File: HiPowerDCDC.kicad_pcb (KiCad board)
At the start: 2 copper layers, 125.8 x 100 mm, 70 parts, among them J1 Conn_01x01, J2 Conn_01x01, J3 Conn_01x01, J4 Conn_01x01, J5 Conn_01x04, J6 Conn_01x02, J7 12V vent., Q1 WMJ38N60, Q2 WMJ38N60, SW1 SW_Push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

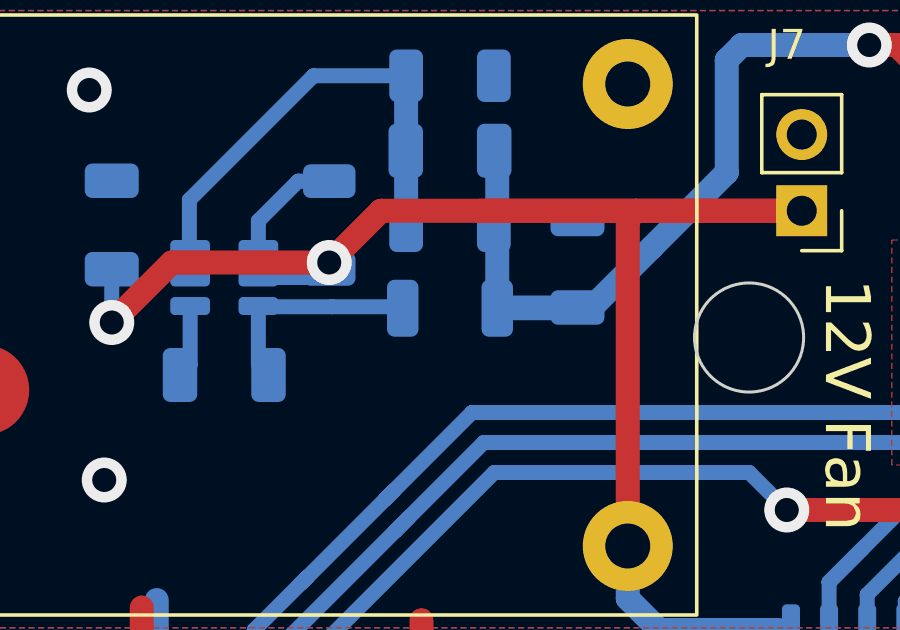
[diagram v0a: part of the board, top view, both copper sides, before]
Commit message: Increased DCDC inductor footprint
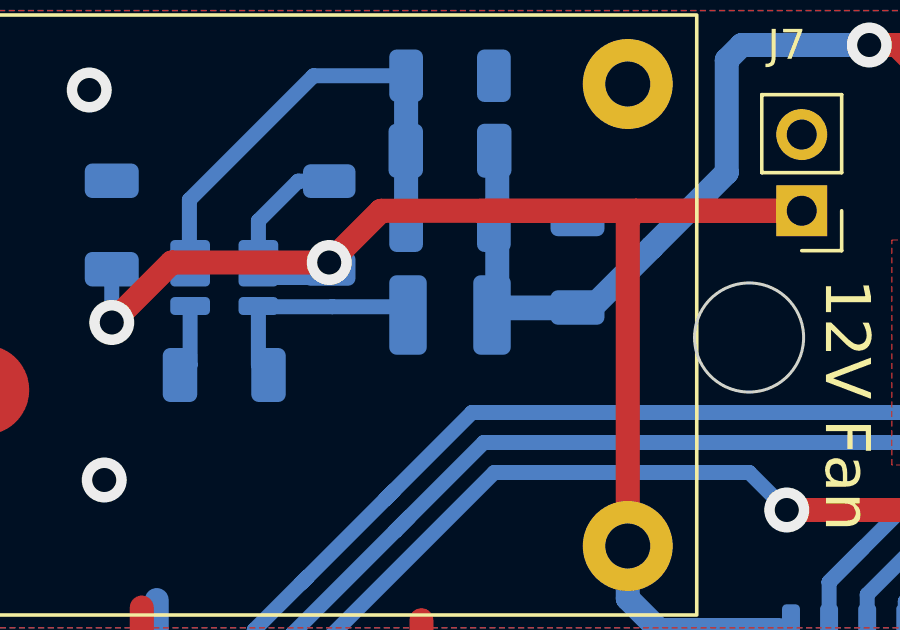
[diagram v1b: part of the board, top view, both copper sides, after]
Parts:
- J7: value 12V vent. -> 12V Fan
- L2: value 2u7 -> 4u7; footprint Inductor_SMD:L_1206_3216Metric -> Inductor_SMD:L_1210_3225Metric
- moved L2 0.22 mm to (132.5, 64.2)
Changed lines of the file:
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@@
       (effects (font (size 1 1) (thickness 0.15)))
     )
-    (fp_text value "12V vent." (at 0 4.87) (layer "F.Fab")
+    (fp_text value "12V Fan" (at 0 4.87) (layer "F.Fab")
       (effects (font (size 1 1) (thickness 0.15)))
     )
@@
     )
   )
-  (footprint "Inductor_SMD:L_1206_3216Metric" (layer "B.Cu")
-    (at 132.525 64.025)
-    (descr "Inductor SMD 1206 (3216 Metric), square (rectangular) end terminal, IPC_7351 nominal, (Body size source: IPC-SM-782 page 80, https://www.pcb-3d.com/wordpress/wp-content/uploads/ipc-sm-782a_amendment_1_and_2.pdf), generated with kicad-footprint-generator")
+  (footprint "Inductor_SMD:L_1210_3225Metric" (layer "B.Cu")
+    (at 132.525 64.25)
+    (descr "Inductor SMD 1210 (3225 Metric), square (rectangular) end terminal, IPC_7351 nominal, (Body size source: http://www.tortai-tech.com/upload/download/2011102023233369053.pdf), generated with kicad-footprint-generator")
     (tags "inductor")
     (property "Sheetfile" "HiPowerDCDC.kicad_sch")
     (property "Sheetname" "")
     (attr smd)
-    (fp_text reference "L2" (at 0 3.725) (layer "B.SilkS")
-      (effects (font (size 1 1) (thickness 0.15)) (justify mirror))
-    )
-    (fp_text value "2u7" (at 0 -1.9) (layer "B.Fab")
-      (effects (font (size 1 1) (thickness 0.15)) (justify mirror))
-    )
-    (fp_text user "${REFERENCE}" (at 0 0) (layer "B.Fab")
-      (effects (font (size 0.8 0.8) (thickness 0.12)) (justify mirror))
-    )
-    (fp_line (start -0.835242 -0.91) (end 0.835242 -0.91) (layer "B.SilkS") (width 0.12))
-    (fp_line (start -0.835242 0.91) (end 0.835242 0.91) (layer "B.SilkS") (width 0.12))
-    (fp_line (start 2.35 1.2) (end 2.35 -1.2) (layer "B.CrtYd") (width 0.05))
-    (fp_line (start -2.35 1.2) (end 2.35 1.2) (layer "B.CrtYd") (width 0.05))
-    (fp_line (start -2.35 -1.2) (end -2.35 1.2) (layer "B.CrtYd") (width 0.05))
-    (fp_line (start 2.35 -1.2) (end -2.35 -1.2) (layer "B.CrtYd") (width 0.05))
-    (fp_line (start -1.6 0.8) (end 1.6 0.8) (layer "B.Fab") (width 0.1))
-    (fp_line (start 1.6 0.8) (end 1.6 -0.8) (layer "B.Fab") (width 0.1))
-    (fp_line (start -1.6 -0.8) (end -1.6 0.8) (layer "B.Fab") (width 0.1))
-    (fp_line (start 1.6 -0.8) (end -1.6 -0.8) (layer "B.Fab") (width 0.1))
-    (pad "1" smd roundrect (at -1.575 0) (size 1.05 1.9) (layers "B.Cu" "B.Paste" "B.Mask") (roundrect_rratio 0.238095)
+    (fp_text reference "L2" (at 0 3.75 180) (layer "B.SilkS")
+      (effects (font (size 1 1) (thickness 0.15)) (justify mirror))
+    )
+    (fp_text value "4u7" (at 0 -2.28 180) (layer "B.Fab")
+      (effects (font (size 1 1) (thickness 0.15)) (justify mirror))
+    )
+    (fp_text user "${REFERENCE}" (at 0 0 180) (layer "B.Fab")
+      (effects (font (size 0.8 0.8) (thickness 0.12)) (justify mirror))
+    )
+    (fp_line (start -0.602064 1.36) (end 0.602064 1.36) (layer "B.SilkS") (width 0.12))
+    (fp_line (start -0.602064 -1.36) (end 0.602064 -1.36) (layer "B.SilkS") (width 0.12))
+    (fp_line (start -2.28 -1.58) (end -2.28 1.58) (layer "B.CrtYd") (width 0.05))
+    (fp_line (start 2.28 1.58) (end 2.28 -1.58) (layer "B.CrtYd") (width 0.05))
+    (fp_line (start 2.28 -1.58) (end -2.28 -1.58) (layer "B.CrtYd") (width 0.05))
+    (fp_line (start -2.28 1.58) (end 2.28 1.58) (layer "B.CrtYd") (width 0.05))
+    (fp_line (start 1.6 -1.25) (end -1.6 -1.25) (layer "B.Fab") (width 0.1))
+    (fp_line (start 1.6 1.25) (end 1.6 -1.25) (layer "B.Fab") (width 0.1))
+    (fp_line (start -1.6 -1.25) (end -1.6 1.25) (layer "B.Fab") (width 0.1))
+    (fp_line (start -1.6 1.25) (end 1.6 1.25) (layer "B.Fab") (width 0.1))
+    (pad "1" smd roundrect (at -1.4 0) (size 1.25 2.65) (layers "B.Cu" "B.Paste" "B.Mask") (roundrect_rratio 0.2)
       (net 55 "Net-(L2-Pad1)") (pinfunction "1") (pintype "passive"))
-    (pad "2" smd roundrect (at 1.575 0) (size 1.05 1.9) (layers "B.Cu" "B.Paste" "B.Mask") (roundrect_rratio 0.238095)
+    (pad "2" smd roundrect (at 1.4 0) (size 1.25 2.65) (layers "B.Cu" "B.Paste" "B.Mask") (roundrect_rratio 0.2)
       (net 58 "+5V") (pinfunction "2") (pintype "passive"))
-    (model "${KICAD6_3DMODEL_DIR}/Inductor_SMD.3dshapes/L_1206_3216Metric.wrl"
+    (model "${KICAD6_3DMODEL_DIR}/Inductor_SMD.3dshapes/L_1210_3225Metric.wrl"
       (offset (xyz 0 0 0))
       (scale (xyz 1 1 1))
@@
     (property "Sheetname" "")
     (attr smd)
-    (fp_text reference "R19" (at 0.025 -4.975) (layer "B.SilkS")
-      (effects (font (size 1 1) (thickness 0.15)) (justify mirror))
-    )
+    (fp_text reference "R19" (at 0.025 -5.225) (layer "B.SilkS")
+      (effects (font (size 1 1) (thickness 0.15)) (justify mirror))
+    )

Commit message: Finished PCB..then Laci started to complain :(
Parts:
- added D4: FR107, Diode_SMD:D_SOD-123, F.Cu at (103.4, 78.0)
- added D5: FR107, Diode_SMD:D_SOD-123, F.Cu at (107.9, 78.0)
- added J8: VDD_BP, Connector_PinSocket_2.54mm:PinSocket_1x01_P2.54mm_Vertical, F.Cu at (113.0, 77.5)
- added J9: VDD_BP, Connector_PinSocket_2.54mm:PinSocket_1x01_P2.54mm_Vertical, F.Cu at (212.8, 90.5)
- moved J7 4.66 mm to (143.2, 56.2), turned to 0 degrees
- moved C1 2.37 mm to (119.0, 60.5)
- moved C17 2.37 mm to (130.3, 58.0)
- moved C18 2.37 mm to (122.8, 65.5)
- moved C3 2.37 mm to (134.5, 61.8)
- moved L2 2.37 mm to (130.3, 63.5)
- moved R19 2.37 mm to (130.3, 60.5)
- moved R20 2.37 mm to (130.3, 55.5)
- moved R21 2.37 mm to (126.2, 60.5)
- moved U4 2.37 mm to (122.8, 62.2)
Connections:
- net Net-(J1-Pad1) renamed VDD
- C17 pad 1: +5V -> +3.3VP
- C3 pad 1: +5V -> +3.3VP
- L2 pad 2: +5V -> +3.3VP
- R19 pad 1: +5V -> +3.3VP
- U2 pad 1: VDC -> Net-(U2-Pad1)
- U5 pad 3: +5V -> +12V
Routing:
- net +5V: track 28.9 -> 0.00 mm, vias 1 -> 0
- net +3.3VP: track 17.2 -> 44.2 mm, vias 0 -> 1
- net Net-(U2-Pad1): track 0.00 -> 23.2 mm
- net VDC: track 44.5 -> 26.1 mm, vias 0 -> 1
- net GND: track 191.0 -> 184.5 mm, vias 8 -> 18
- net Net-(D5-Pad2): track 0.00 -> 5.99 mm
- net VCC: track 15.0 -> 17.0 mm, vias 0 -> 1
- net +12V: track 64.7 -> 63.0 mm
- net VIN: track 75.4 -> 76.6 mm
- net Net-(U1-Pad37): track 62.4 -> 63.3 mm
- removed copper zone on F.Cu, net Net-(C11-Pad1)
- removed copper zone on F.Cu, net VCC
- removed copper zone on F.Cu, net VDC
- removed copper zone on F.Cu, net VDD
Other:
- board text added: "3V3 EN"
- board text added: "Bypass with J8"
- board text removed: "3V3 PS"

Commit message: Laci, do you want me to re design the whole f*kin PCB?
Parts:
- added R23: 330k, Resistor_SMD:R_1206_3216Metric, B.Cu at (112.0, 85.3)
- added R24: 330k, Resistor_SMD:R_1206_3216Metric, B.Cu at (112.0, 80.3)
- added R25: 330k, Resistor_SMD:R_1206_3216Metric, B.Cu at (211.3, 90.7)
- added R26: 330k, Resistor_SMD:R_1206_3216Metric, B.Cu at (211.3, 80.1)
- R10: value 10M -> 1M; footprint Resistor_SMD:R_1812_4532Metric -> Resistor_THT:R_Axial_DIN0207_L6.3mm_D2.5mm_P10.16mm_Horizontal; moved to F.Cu
- R11, R13: value 1M -> 330k
- moved R10 22.1 mm to (118.0, 120.2)
- moved R13 7.48 mm to (112.0, 90.7)
- moved J9 3.90 mm to (212.8, 94.4)
- moved D4 3.80 mm to (103.4, 74.2)
- moved D5 3.80 mm to (107.9, 74.2)
- moved J8 3.80 mm to (113.0, 73.7)
- moved R11 2.20 mm to (211.3, 85.2), turned to 0 degrees
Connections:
- R11 pad 1: VDD -> Net-(R11-Pad1)
- R11 pad 2: VOUT -> Net-(R11-Pad2)
- R13 pad 2: VIN -> Net-(R13-Pad2)
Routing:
- net VDD: track 20.9 -> 13.4 mm
- net Net-(R11-Pad1): track 0.00 -> 5.50 mm
- net Net-(R13-Pad2): track 0.00 -> 5.40 mm
- net Net-(R11-Pad2): track 0.00 -> 5.10 mm
- net Net-(R23-Pad2): track 0.00 -> 5.00 mm
- net Net-(D4-Pad1): track 23.2 -> 18.7 mm
- net VIN: track 76.6 -> 78.7 mm
- net VOUT: track 50.6 -> 51.9 mm
- net VDC: track 26.1 -> 27.2 mm

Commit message: Finalized PCB
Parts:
- added C19: 1u, Capacitor_THT:C_Rect_L26.5mm_W11.5mm_P22.50mm_MKS4, F.Cu at (75.8, 88.8)
- added C20: 1u, Capacitor_THT:C_Rect_L26.5mm_W11.5mm_P22.50mm_MKS4, F.Cu at (63.2, 106.2)
- added C21: 1u, Capacitor_THT:C_Rect_L26.5mm_W11.5mm_P22.50mm_MKS4, F.Cu at (108.8, 114.8)
- added F1: Fuse, Laci:Fuseholder_Schurter_0751.0505, F.Cu at (90.8, 103.3)
- added GD1: GDT_2Pin, HiPowerFP:CG2-350L, F.Cu at (72.8, 121.0)
- added J10: Conn_01x01, HiPowerFP:Keystone_7808, F.Cu at (58.8, 92.5)
- added RV1: V275LA20AP, Varistor:RV_Disc_D15.5mm_W3.9mm_P7.5mm, F.Cu at (88.0, 110.3)
- added RV2: V275LA20AP, Varistor:RV_Disc_D15.5mm_W3.9mm_P7.5mm, F.Cu at (99.5, 125.2)
- moved J3 69.2 mm to (58.8, 64.0)
- moved J2 52.0 mm to (58.8, 142.0)
- moved D4 6.16 mm to (103.8, 80.3)
- moved R24 4.95 mm to (115.5, 83.8), turned to 90 degrees
- moved R23 4.81 mm to (115.5, 88.6), turned to 90 degrees
- moved R13 4.42 mm to (115.5, 93.4), turned to 90 degrees
- moved R26 4.14 mm to (208.7, 83.2), turned to 90 degrees
- moved R11 3.92 mm to (208.7, 88.0), turned to 90 degrees
- moved R25 3.44 mm to (208.7, 92.8), turned to 90 degrees
- moved J8 3.30 mm to (113.0, 77.0)
- moved C14 3.28 mm to (130.8, 125.6)
- moved C10 3.28 mm to (138.8, 125.6)
- moved C12 3.28 mm to (134.8, 125.6)
- moved D5 2.93 mm to (108.8, 77.0), turned to 0 degrees
- moved R10 1.88 mm to (117.2, 121.9)
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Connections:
- C4 pad 2: GND -> unconnected-(C4-Pad2)
- J3 pad 1: VDC -> Net-(F1-Pad2)
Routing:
- net VDC: track 27.2 -> 85.6 mm
- net GND: track 184.5 -> 198.4 mm
- net VCC: track 17.0 -> 24.9 mm
- net Net-(D4-Pad1): track 18.7 -> 24.2 mm
- net VIN: track 78.7 -> 74.5 mm
- net Net-(R11-Pad1): track 5.50 -> 1.88 mm
- net VOUT: track 51.9 -> 48.3 mm
- net Net-(R13-Pad2): track 5.40 -> 1.88 mm
- net Net-(D5-Pad2): track 5.99 -> 2.60 mm
- net VDD: track 13.4 -> 10.1 mm
- net Net-(R11-Pad2): track 5.10 -> 1.88 mm
- net Net-(R23-Pad2): track 5.00 -> 1.88 mm
- net Earth: track 0.00 -> 2.83 mm
- added copper zone on B.Cu, net Earth
- added copper zone on F.Cu, net Earth
- added copper zone on B.Cu, net Net-(F1-Pad2)
- added copper zone on F.Cu, net Net-(F1-Pad2)
- added copper zone on B.Cu, net Net-(GD1-Pad2)
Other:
- board size 125.8 x 100 mm -> 175.8 x 100 mm
- board text added: "PE"
